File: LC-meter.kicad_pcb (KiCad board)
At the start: 2 copper layers, 39 parts, among them J1 ResetSW, J2 ICSP, J3 1RowDsp, J4 OscTest, J5 Display, J6 Backled, J7 Power, J8 L/C, J9 L/C Switch, K1 SIP-1A05D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

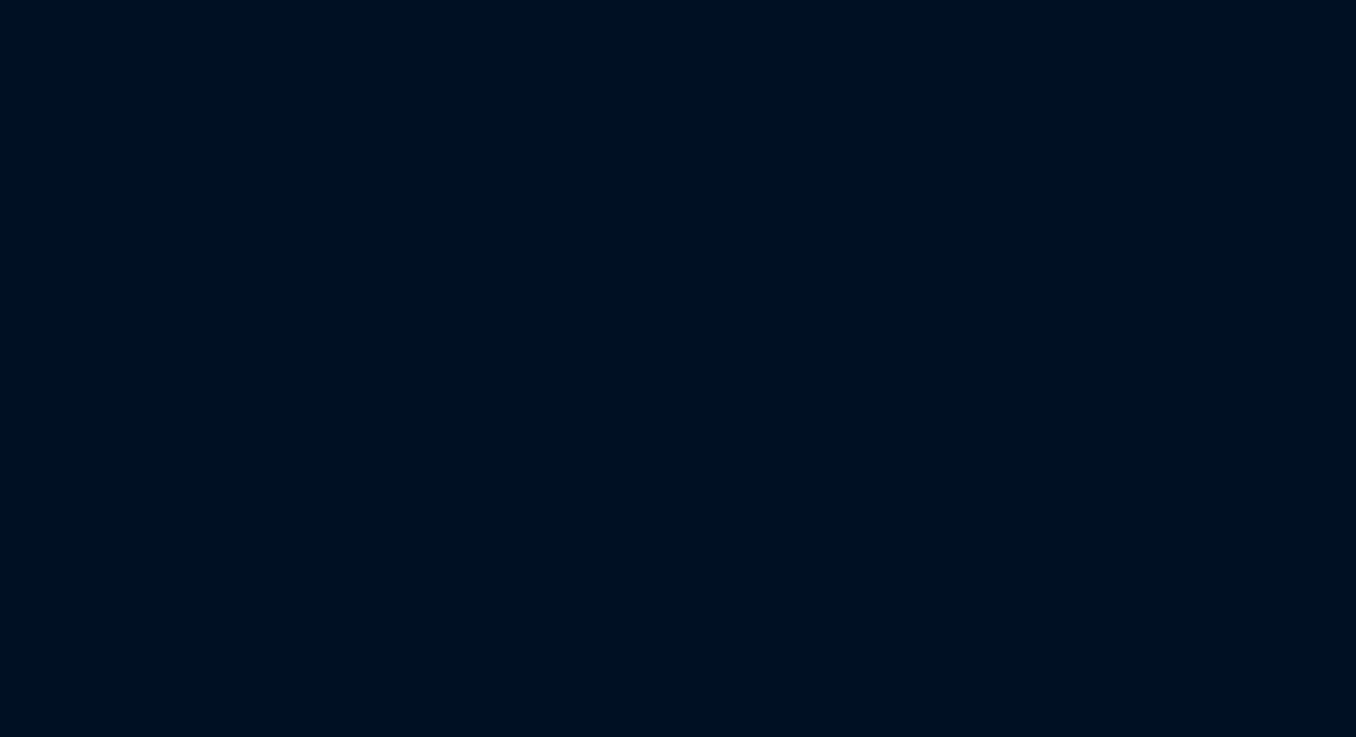
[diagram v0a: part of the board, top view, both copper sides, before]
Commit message: add display
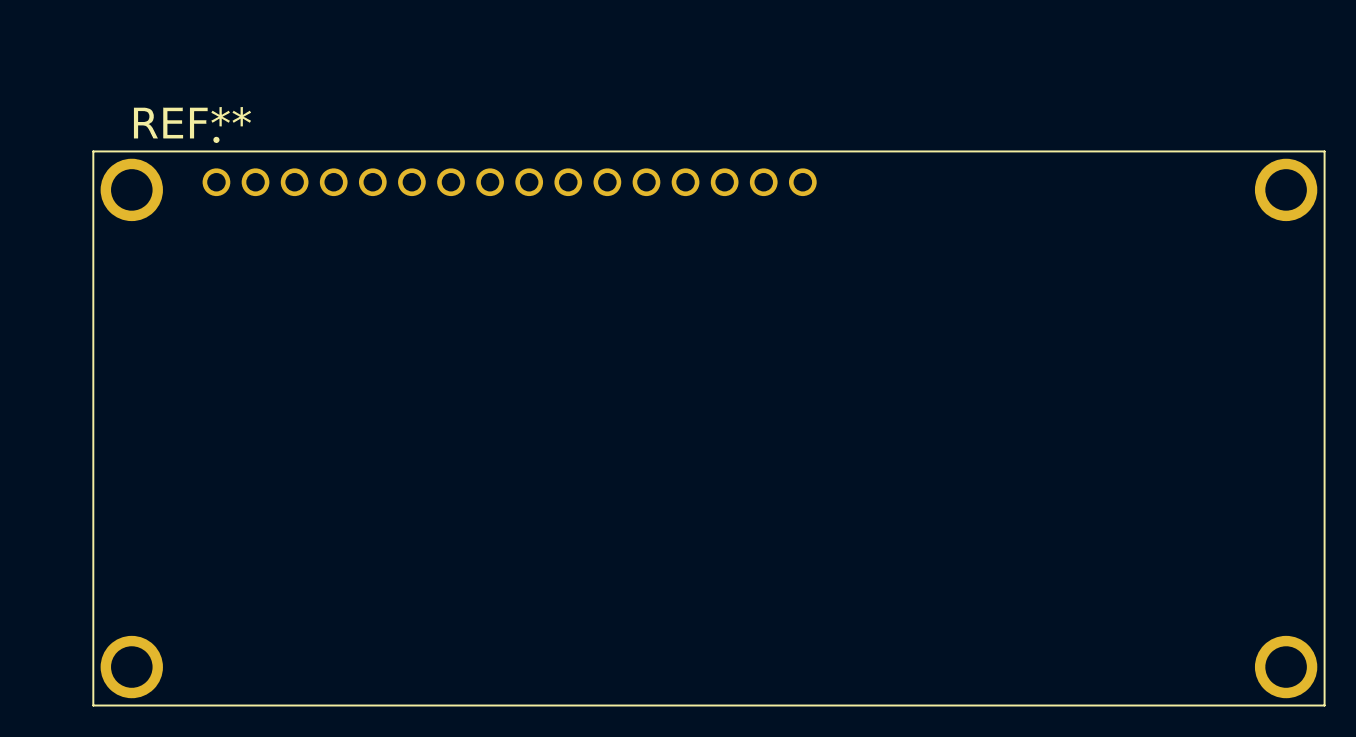
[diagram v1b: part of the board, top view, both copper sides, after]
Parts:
- added REF**: NHD_NHD-0216K1Z-NSW-BBW-L, TQ2SA-5V:NHD_NHD-0216K1Z-NSW-BBW-L, F.Cu at (212.1, 90.6)

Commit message: 11-10-2024
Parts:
- U1: moved to B.Cu
- moved R3 78.6 mm to (140.2, 56.4), turned to -90 degrees
- moved C2 78.5 mm to (39.5, 83.3)
- moved J7 78.5 mm to (32.3, 81.9)
- moved C10 78.5 mm to (71.9, 83.1)
- moved C11 78.5 mm to (76.7, 83.0)
- moved U2 78.5 mm to (45.5, 79.3)
- moved C1 78.5 mm to (36.0, 81.5)
- moved C3 78.5 mm to (58.0, 83.4)
- moved C4 78.5 mm to (52.2, 81.8)
- moved Y1 63.0 mm to (125.9, 84.3)
- moved C6 62.8 mm to (132.9, 89.4), turned to 180 degrees
- moved C5 62.6 mm to (118.9, 89.4), turned to 0 degrees
- moved D1 57.9 mm to (139.2, 59.4)
- moved J3 43.2 mm to (154.7, 56.4)
- moved U1 41.2 mm to (132.8, 73.5), turned to -90 degrees
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
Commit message: 11-10-2024 PCB ready
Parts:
- removed the REF** at (235.2, 100.1)
- added REF**: MountingHole_2.7mm_M2.5_DIN965_Pad, MountingHole:MountingHole_2.7mm_M2.5_DIN965_Pad, F.Cu at (102.2, 63.5)
- added REF**: MountingHole_2.7mm_M2.5_DIN965_Pad, MountingHole:MountingHole_2.7mm_M2.5_DIN965_Pad, F.Cu at (102.2, 94.5)
- added REF**: MountingHole_2.7mm_M2.5_DIN965_Pad, MountingHole:MountingHole_2.7mm_M2.5_DIN965_Pad, F.Cu at (177.2, 94.5)
- added REF**: MountingHole_2.7mm_M2.5_DIN965_Pad, MountingHole:MountingHole_2.7mm_M2.5_DIN965_Pad, F.Cu at (177.2, 63.5)
- J1, J2, J7, J8, J9: moved to B.Cu
- moved K2 125.5 mm to (160.4, 82.7)
- moved J8 117.6 mm to (175.3, 56.5), turned to 180 degrees
- moved J9 106.7 mm to (168.7, 56.6), turned to 180 degrees
- moved L1 99.0 mm to (151.2, 80.5), turned to -90 degrees
- moved R2 97.0 mm to (150.9, 85.2)
- moved R6 96.1 mm to (157.4, 69.2), turned to 90 degrees
- moved R7 93.3 mm to (155.2, 73.2), turned to 90 degrees
- moved R8 91.4 mm to (155.2, 69.2), turned to 90 degrees
- moved R5 90.0 mm to (146.1, 87.5), turned to 180 degrees
- moved R9 87.0 mm to (146.1, 85.2)
- moved R4 79.9 mm to (139.6, 71.8), turned to 90 degrees
- moved C9 78.0 mm to (136.9, 85.2)
- moved J7 71.7 mm to (103.2, 71.4), turned to 180 degrees
- moved C1 70.9 mm to (106.9, 81.3), turned to -90 degrees
- moved R10 70.0 mm to (128.2, 86.0), turned to 90 degrees
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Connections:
- J4 pad 1: RB6 -> GND
- J4 pad 2: GND -> RB6
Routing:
- net +5V: track 0.00 -> 154.9 mm, vias 0 -> 1
- net RA4: track 0.00 -> 46.6 mm, vias 0 -> 1
- net PGD: track 0.00 -> 45.5 mm, vias 0 -> 1
- net PGC: track 0.00 -> 40.9 mm, vias 0 -> 1
- net Net-(C8-Pad2): track 0.00 -> 35.7 mm
- net L/C: track 0.00 -> 27.8 mm
- net RB4: track 0.00 -> 27.3 mm
- net Net-(U3-+): track 0.00 -> 26.8 mm, vias 0 -> 2
- net Net-(R4-Pad2): track 0.00 -> 21.7 mm
- net L/C SW: track 0.00 -> 19.9 mm
- net RB6: track 0.00 -> 18.7 mm
- net VPP/MCRL: track 0.00 -> 16.9 mm, vias 0 -> 1
- net Net-(K2-Pad2): track 0.00 -> 16.8 mm, vias 0 -> 2
- net Net-(U1-OSC1/CLKIN): track 0.00 -> 15.7 mm, vias 0 -> 1
- net RA3: track 0.00 -> 14.8 mm, vias 0 -> 1
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- added copper zone on B.Cu, net GND
- added copper zone on F.Cu, net GND
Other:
- board outline added: 81.1 x 45.2 mm
- board text added: "+ -"
- board text added: "="
- board text added: "J1,J7,J8,J9"
- board text added: "J2 1 = VPP/MCRL 2 = +5V 3 = GND 4 = PGD 5 = PGC 6 = NC"
- board text added: "Made By PA2ER.NL 10-2024 V1.0"

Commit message: Update 23-10-2024
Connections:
- U3 pad 5: unconnected-(U3-BAL-Pad5) -> Net-(U3-BAL)
- U3 pad 6: unconnected-(U3-STRB-Pad6) -> Net-(U3-BAL)
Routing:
- net Net-(U3-BAL): track 0.00 -> 1.27 mm
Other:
- board text added: "J9-2 to ground = Induction"
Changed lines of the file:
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@@
 	(net 36 "unconnected-(U1-RB5-Pad11)")
 	(net 37 "RA1")
-	(net 38 "unconnected-(U3-STRB-Pad6)")
-	(net 39 "unconnected-(U3-BAL-Pad5)")
-	(net 40 "unconnected-(J2-Pin_6-Pad6)")
-	(net 41 "Net-(K1-Pad3)")
+	(net 38 "Net-(U3-BAL)")
+	(net 39 "unconnected-(J2-Pin_6-Pad6)")
+	(net 40 "Net-(K1-Pad3)")
 	(footprint "Capacitor_Tantalum_SMD:CP_EIA-6032-28_Kemet-C_Pad2.25x2.35mm_HandSolder"
 		(layer "F.Cu")
@@
 		(tags "resistor handsolder")
 		(property "Reference" "R5"
-			(at -3.05 -0.15 360)
+			(at -3.05 -0.15 0)
 			(layer "F.SilkS")
 			(effects
@@
 		)
 		(property "Value" "100K"
-			(at 0 1.65 360)
+			(at 0 1.65 0)
 			(layer "F.Fab")
 			(effects
@@
 		)
 		(fp_text user "${REFERENCE}"
-			(at 0 0 360)
+			(at 0 0 0)
 			(layer "F.Fab")
 			(effects
@@
 		(tags "Through hole pin header THT 1x02 2.54mm single row")
 		(property "Reference" "J3"
-			(at -0.05 -3.012 360)
+			(at -0.05 -3.012 0)
 			(layer "F.SilkS")
 			(effects
@@
 		)
 		(property "Value" "1RowDsp"
-			(at -1.8 5.138 360)
+			(at -1.8 5.138 0)
 			(layer "F.SilkS")
 			(effects
@@
 			(layers "F.Cu" "F.Paste" "F.Mask")
 			(roundrect_rratio 0.208333)
-			(net 41 "Net-(K1-Pad3)")
+			(net 40 "Net-(K1-Pad3)")
 			(pintype "passive")
 		)
@@
 			(layers "*.Cu" "*.Mask")
 			(remove_unused_layers no)
-			(net 41 "Net-(K1-Pad3)")
+			(net 40 "Net-(K1-Pad3)")
 			(pintype "passive")
 		)
@@
 		(tags "capacitor handsolder")
 		(property "Reference" "C11"
-			(at 3.3625 0 360)
+			(at 3.3625 0 0)
 			(layer "F.SilkS")
 			(effects
@@
 		)
 		(property "Value" "1000pF"
-			(at 0 1.68 360)
+			(at 0 1.68 0)
 			(layer "F.Fab")
 			(effects
@@
 		)
 		(fp_text user "${REFERENCE}"
-			(at 0 0 360)
+			(at 0 0 0)
 			(layer "F.Fab")
 			(effects
@@
 		(tags "capacitor handsolder")
 		(property "Reference" "C10"
-			(at 3.3625 -0.1 360)
+			(at 3.3625 -0.1 0)
 			(layer "F.SilkS")
 			(effects
@@
 		)
 		(property "Value" "100pF"
-			(at 4.3625 0.15 360)
+			(at 4.3625 0.15 0)
 			(layer "F.Fab")
 			(effects
@@
 		)
 		(fp_text user "${REFERENCE}"
-			(at 0 0 360)
+			(at 0 0 0)
 			(layer "F.Fab")
 			(effects
@@
 			(layers "F.Cu" "F.Paste" "F.Mask")
 			(roundrect_rratio 0.25)
-			(net 39 "unconnected-(U3-BAL-Pad5)")
+			(net 38 "Net-(U3-BAL)")
 			(pinfunction "BAL")
-			(pintype "input+no_connect")
+			(pintype "input")
 		)
 		(pad "6" smd roundrect
@@
 			(layers "F.Cu" "F.Paste" "F.Mask")
 			(roundrect_rratio 0.25)
-			(net 38 "unconnected-(U3-STRB-Pad6)")
+			(net 38 "Net-(U3-BAL)")
 			(pinfunction "STRB")
-			(pintype "input+no_connect")
+			(pintype "input")
 		)
 		(pad "7" smd roundrect
@@
 		(tags "Through hole pin header THT 1x02 2.54mm single row")
 		(property "Reference" "J4"
-			(at -0.048 -3.012 360)
+			(at -0.048 -3.012 0)
 			(layer "F.SilkS")
 			(effects
@@
 		)
 		(property "Value" "OscTest"
-			(at 1.052 5.188 360)
+			(at 1.052 5.188 0)
 			(layer "F.SilkS")
 			(effects
@@
 		)
 		(property "Value" "ICSP"
-			(at 2.55 -6.35 360)
+			(at 2.55 -6.35 0)
 			(layer "B.SilkS")
 			(effects
@@
 		)
 		(fp_text user "${REFERENCE}"
-			(at 0 -6.35 360)
+			(at 0 -6.35 0)
 			(layer "B.Fab")
 			(effects
@@
 			(layers "*.Cu" "*.Mask")
 			(remove_unused_layers no)
-			(net 40 "unconnected-(J2-Pin_6-Pad6)")
+			(net 39 "unconnected-(J2-Pin_6-Pad6)")
 			(pinfunction "Pin_6")
 			(pintype "passive+no_connect")
@@
 		)
 	)
+	(gr_text "J9-2 to ground = Induction"
+		(at 169.05 72.45 0)
+		(layer "B.SilkS")
+		(effects
+			(font
+				(size 1 1)
+				(thickness 0.1)
+			)
+			(justify left bottom mirror)
+		)
+	)
 	(gr_text "="
 		(at 173.25 69.75 0)
@@
 	)
 	(segment
+		(start 144.03 69.7)
+		(end 145.3 69.7)
+		(width 0.2)
+		(layer "F.Cu")
+		(net 38)
+	)
+	(segment
 		(start 128.25 80.97)
 		(end 128.18 80.9)
 		(width 0.2)
 		(layer "F.Cu")
-		(net 41)
+		(net 40)
 	)
 	(segment
@@
 		(width 0.2)
 		(layer "F.Cu")
-		(net 41)
+		(net 40)
 	)
 	(zone
